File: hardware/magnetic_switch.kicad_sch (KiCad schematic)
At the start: 15 parts, among them J1 Conn_01x01_Socket, J2 Conn_01x01_Socket, J3 Conn_01x01_Socket, J4 Conn_01x01_Socket, Q1 SiA449DJ, Q2 BC847W, U1 DRV5012, U2 TPS70933

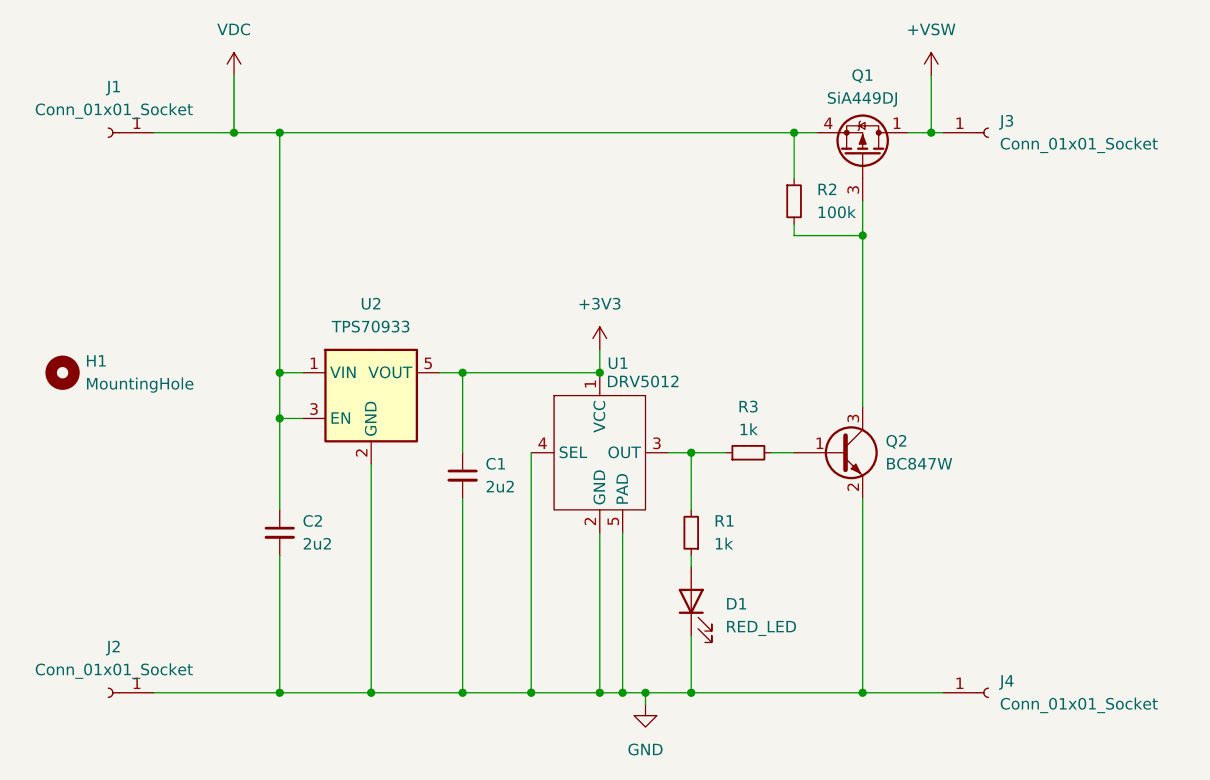
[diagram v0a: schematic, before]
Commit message: Minor cleanup of the schematic
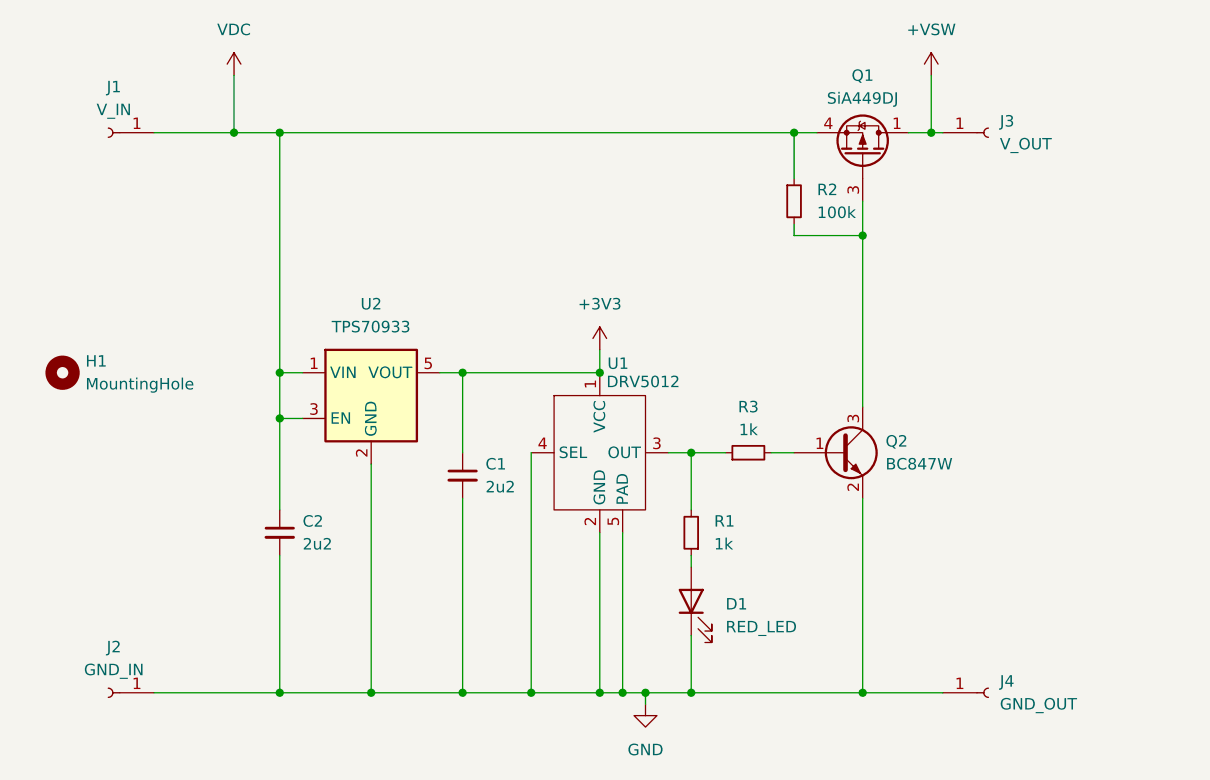
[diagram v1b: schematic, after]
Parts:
- J1: value Conn_01x01_Socket -> V_IN
- J2: value Conn_01x01_Socket -> GND_IN
- J3: value Conn_01x01_Socket -> V_OUT
- J4: value Conn_01x01_Socket -> GND_OUT
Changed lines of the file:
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@@
 			)
 		)
-		(property "Value" "Conn_01x01_Socket"
+		(property "Value" "GND_IN"
 			(at 59.055 97.79 0)
 			(effects
@@
 			)
 		)
-		(property "Value" "Conn_01x01_Socket"
+		(property "Value" "V_OUT"
 			(at 157.48 39.3699 0)
 			(effects
@@
 			)
 		)
-		(property "Value" "Conn_01x01_Socket"
+		(property "Value" "GND_OUT"
 			(at 157.48 101.5999 0)
 			(effects
@@
 			)
 		)
-		(property "Value" "Conn_01x01_Socket"
+		(property "Value" "V_IN"
 			(at 59.055 35.56 0)
 			(effects

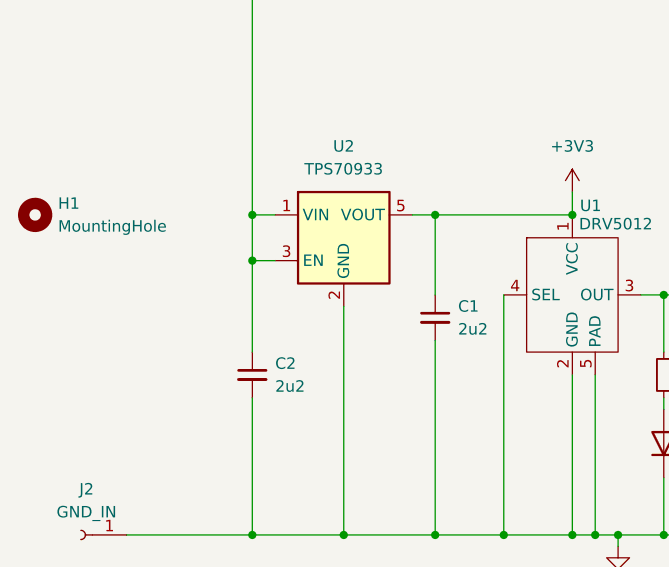
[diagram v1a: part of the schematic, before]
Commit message: Corrected issue with regulator enable pin which needs to be left floating, NOT tied to VCC and updated README to reflect the fact that testing is complete.
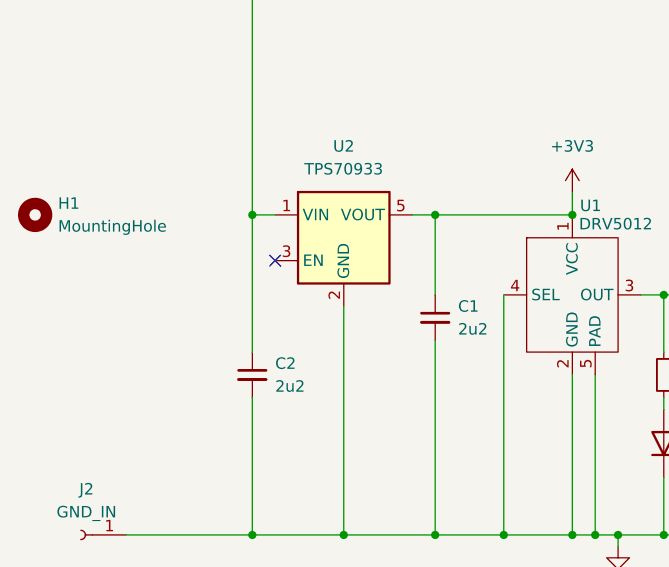
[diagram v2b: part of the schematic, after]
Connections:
- net VDC: no longer U2.3 (EN)
- no-connect marks 0 -> 1
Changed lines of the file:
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@@
-	)
-	(junction
-		(at 77.47 69.85)
-		(diameter 0)
-		(color 0 0 0 0)
 	)
 	(junction
@@
 		(color 0 0 0 0)
 	)
+	(no_connect
+		(at 80.01 69.85)
+	)
 	(wire
 		(pts
@@
 	(wire
 		(pts
-			(xy 77.47 69.85) (xy 77.47 64.77)
+			(xy 77.47 64.77) (xy 77.47 80.01)
 		)
 		(stroke
@@
 		)
 		(stroke
-			(width 0)
-			(type default)
-		)
-	)
-	(wire
-		(pts
-			(xy 80.01 69.85) (xy 77.47 69.85)
-		)
-		(stroke
-			(width 0)
-			(type default)
-		)
-	)
-	(wire
-		(pts
-			(xy 77.47 69.85) (xy 77.47 80.01)
-		)
-		(stroke

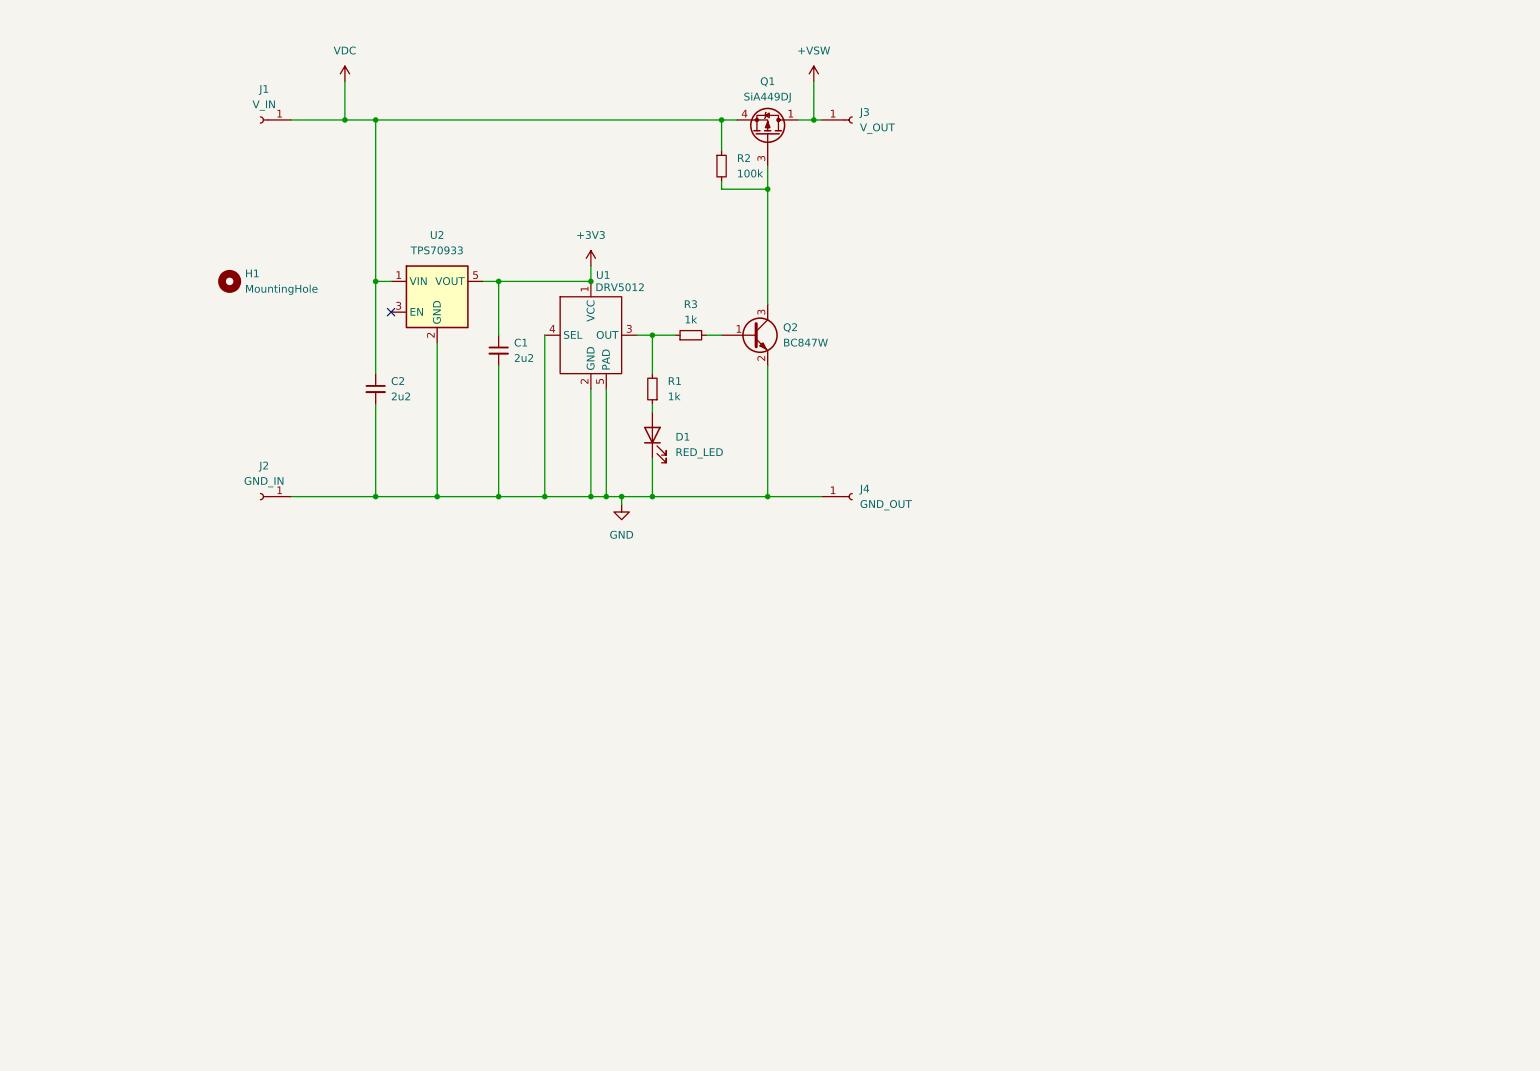
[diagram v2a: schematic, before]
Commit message: updated to smaller components and re-layed out.
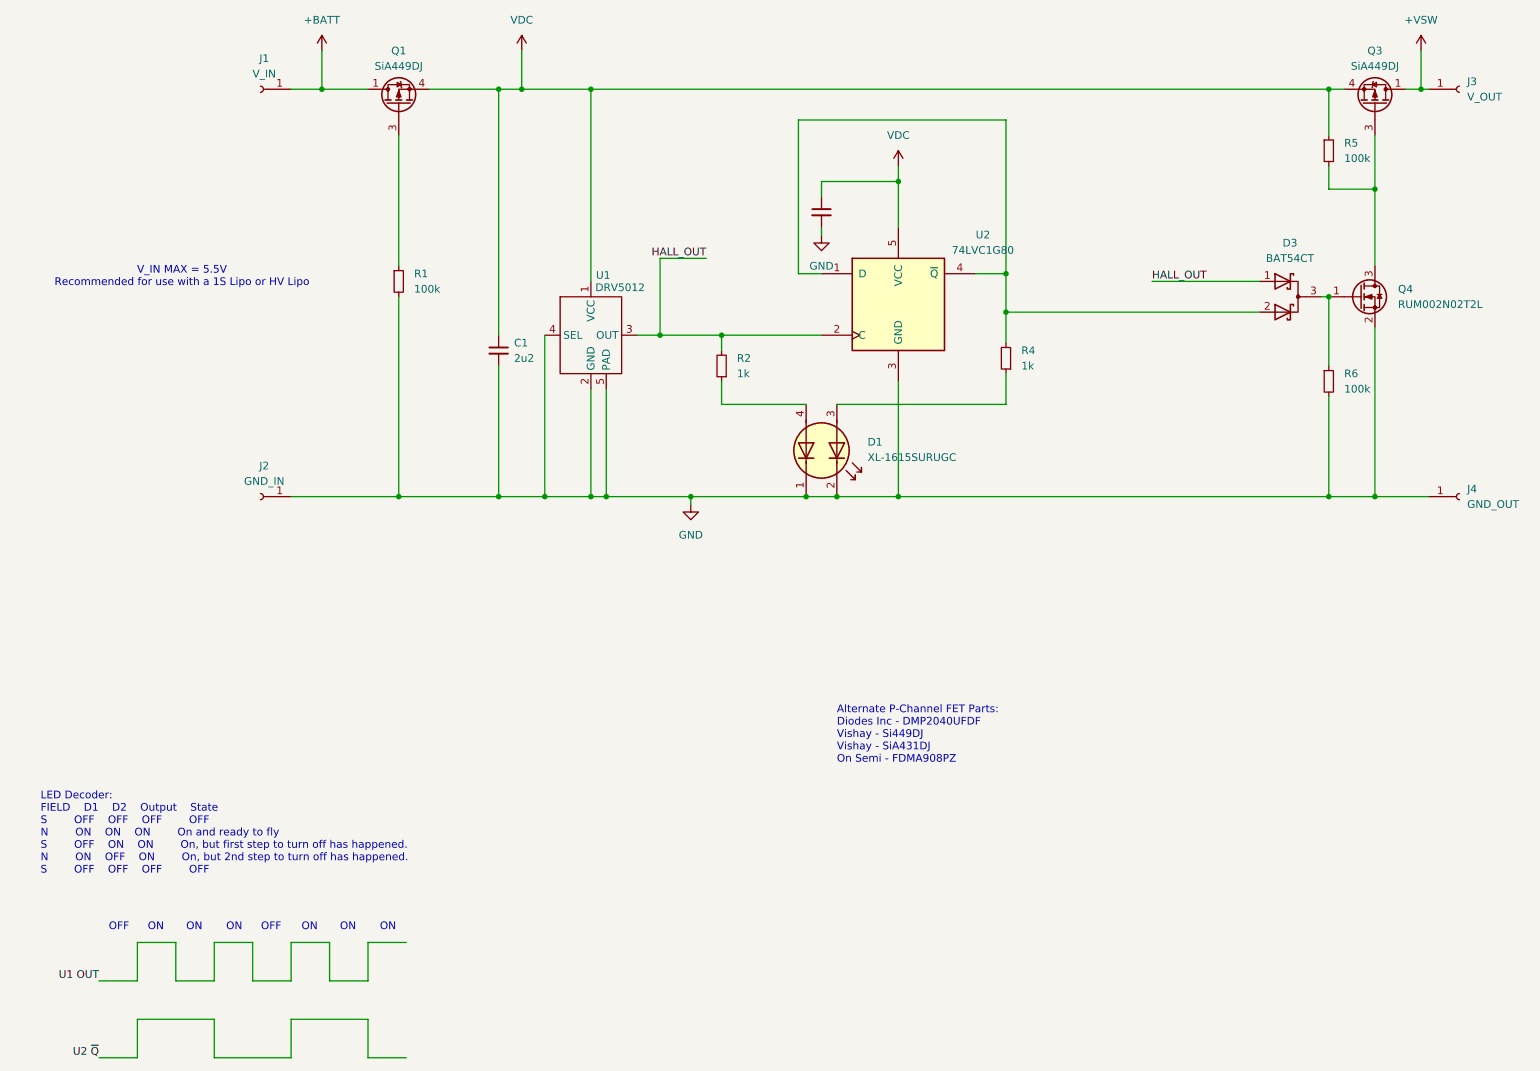
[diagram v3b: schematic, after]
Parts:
- removed D1: RED_LED, LED_SMD:LED_0402_1005Metric, symbol Device:LED
- removed H1: MountingHole, MountingHole:MountingHole_2.2mm_M2_DIN965_Pad, symbol Mechanical:MountingHole
- removed Q2: BC847W, Package_TO_SOT_SMD:SOT-323_SC-70, symbol Transistor_BJT:BC847W
- removed R3: 1k, Resistor_SMD:R_0402_1005Metric, symbol Device:R_Small
- removed U2: TPS70933, Package_TO_SOT_SMD:SOT-23-5, symbol Regulator_Linear:NCP163ASN330T1G
- added D1: XL-1615SURUGC, Footprints:LED_SMT_DUAL_1615, symbol My Components:LED_Dual_KKAA
- added D3: BAT54CT, Package_TO_SOT_SMD:SOT-523, symbol Device:D_Schottky_Dual_CommonCathode_AAK_Parallel
- added Q1: SiA449DJ, Package_TO_SOT_SMD:Vishay_PowerPAK_SC70-6L_Single, symbol Transistor_FET:SiA449DJ
- added Q4: RUM002N02T2L, Package_TO_SOT_SMD:SOT-723, symbol Transistor_FET:Q_NMOS_GSD
- added R1, R6: 100k, Resistor_SMD:R_0402_1005Metric, symbol Device:R_Small
- added R4: 1k, Resistor_SMD:R_0402_1005Metric, symbol Device:R_Small
- added U2: 74LVC1G80, Package_TO_SOT_SMD:SOT-353_SC-70-5, symbol 74xGxx:74LVC1G80
- C2: value 2u2 -> 100n
- J1, J2, J3, J4: footprint My Footprints:WireSolderPad_w_hole -> MountingHole:MountingHole_2.2mm_M2_DIN965_Pad
- U1: footprint My Footprints:X2SON_4_EP -> Footprints:X2SON_4_EP
- renumbered Q1 to Q3, R1 to R2, R2 to R5
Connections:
- net +3V3 is gone; now on net VDC: C1.1, U1.1 (VCC)
- net GND: now also D1.1 (K2), D1.2 (K1), Q4.2 (S), R1.2, R6.2, U2.3 (GND)
- net VDC: now also Q1.4 (S), U2.5 (VCC); no longer J1.1 (Pin_1)
- net at R2.1: now also D1.4 (A2)
- net HALL_OUT: now reaches R2.2, U1.3 (OUT)
- net HALL_OUT: now also D3.1 (A), U2.2 (C)
- net at Q3.3 (G), R5.2: now also Q4.3 (D)
- new net: D1.3 (A1), R4.1
- new net: D3.2 (A), R4.2, U2.1 (D), U2.4 (~{Q})
- new net: D3.3 (K), Q4.1 (G), R6.1
- new net: Q1.3 (G), R1.1
- new net +BATT: J1.1 (Pin_1), Q1.1 (D)
- no-connect marks 1 -> 0
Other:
- note added: "Alternate P-Channel FET Parts: Diodes Inc - DMP2040UFDF Vishay - Si449DJ Vishay - SiA431DJ On Semi - FDMA908PZ"
- note added: "LED Decoder: FIELD D1 D2 Output State S OFF OFF OFF OFF N ON ON ON On and ready to fly S OFF ON ON On, but first step to turn off has happened. N ON OFF ON On, but 2nd step to turn off has happened. S OFF OFF OFF OFF"
- note added: "OFF"
- note added: "ON"
- note added: "V_IN MAX = 5.5V Recommended for use with a 1S Lipo or HV Lipo"
- title: SimpleSwitch -> MagSafeSwitch
- moved on the sheet: J1, J3, J4, Q3, R2, R5

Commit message: added a linear regulator to allow up to +12V input. This version was sent for manufacture.
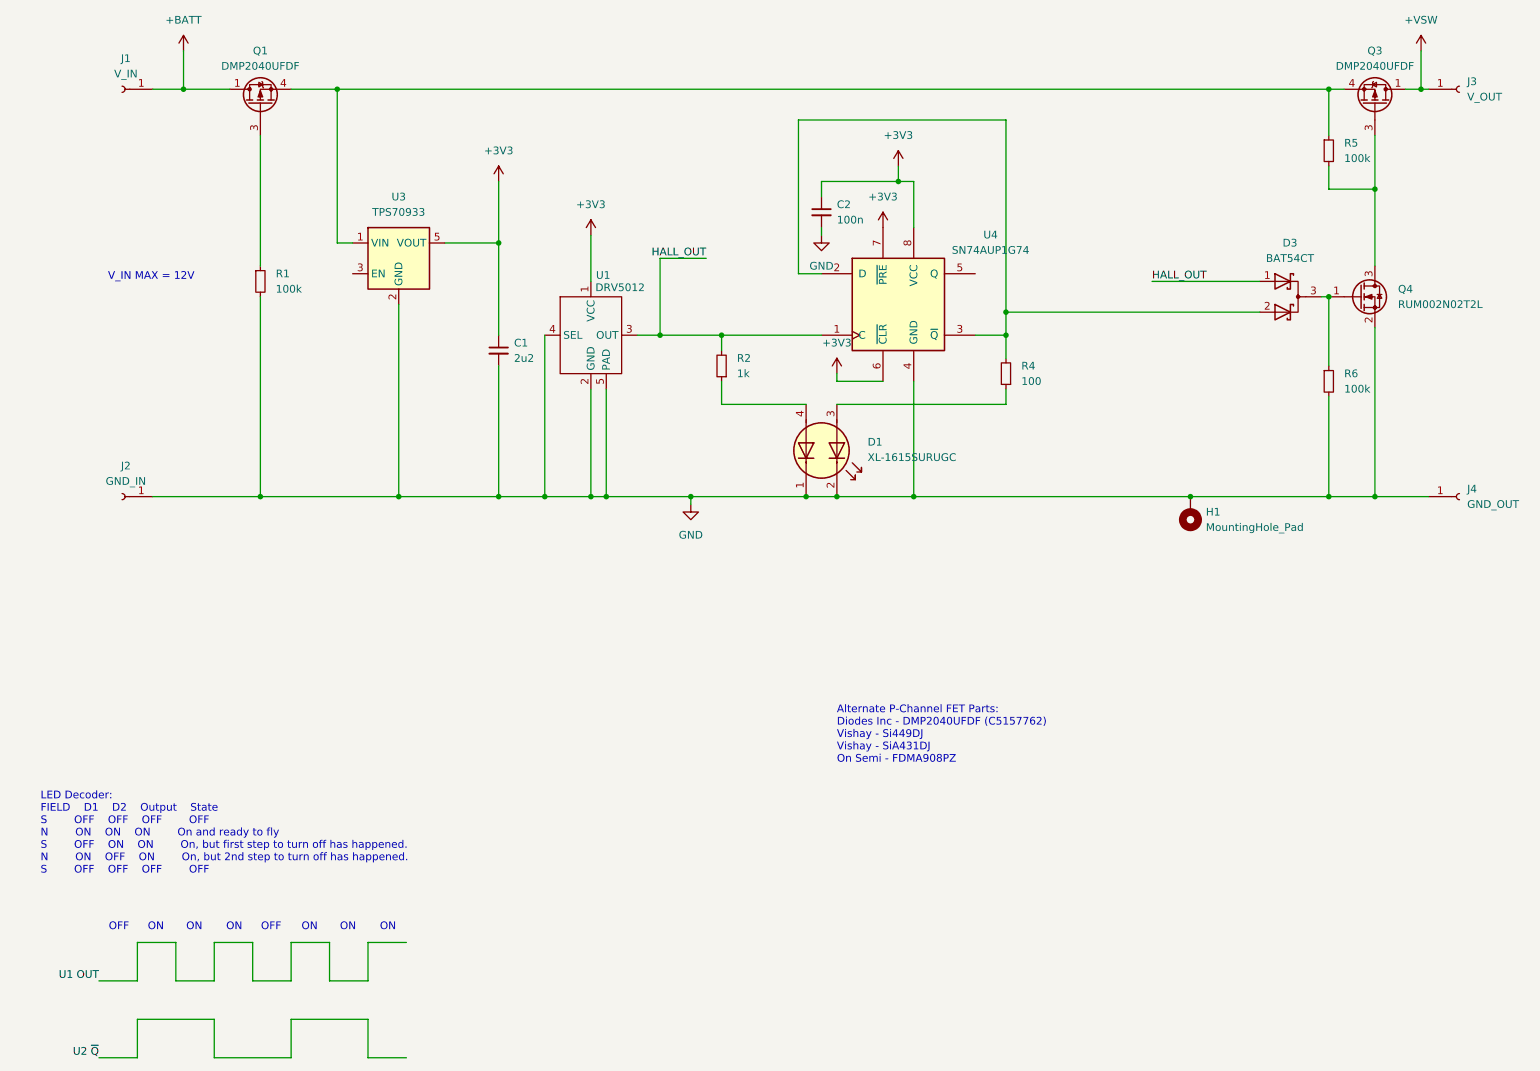
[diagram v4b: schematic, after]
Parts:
- removed U2: 74LVC1G80, Package_TO_SOT_SMD:SOT-353_SC-70-5, symbol 74xGxx:74LVC1G80
- added H1: MountingHole_Pad, MountingHole:MountingHole_2.2mm_M2_DIN965_Pad, symbol Mechanical:MountingHole_Pad
- added U3: TPS70933, Package_TO_SOT_SMD:SOT-23-5, symbol Regulator_Linear:NCP163ASN330T1G
- added U4: SN74AUP1G74, Package_SON:X2SON-8_1.4x1mm_P0.35mm, symbol 74xGxx:74AUP1G74
- D1: JLCPCB Part # (none) -> C965839
- D3: JLCPCB Part # (none) -> C134407
- J1, J2, J3, J4: footprint MountingHole:MountingHole_2.2mm_M2_DIN965_Pad -> Footprints:WireSolderPad_w_hole
- Q1, Q3: value SiA449DJ -> DMP2040UFDF; JLCPCB Part # (none) -> C5157762
- Q4: JLCPCB Part # (none) -> C250130
- R4: value 1k -> 100
- U1: JLCPCB Part # (none) -> C2655038
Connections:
- net GND: now also H1.1, U3.2 (GND), U4.4 (GND)
- net HALL_OUT: now also U4.1 (C)
- net at D3.2 (A), R4.2: now also U4.2 (D), U4.3 (~{Q})
- net VDC: no longer names the net of Q1.4 (S), Q3.4 (S), R5.1
- net VDC: now also U3.1 (VIN); no longer C1.1, C2.1, U1.1 (VCC)
- new net +3V3: C1.1, C2.1, U1.1 (VCC), U3.5 (VOUT), U4.6 (~{CLR}), U4.7 (~{PRE}), U4.8 (VCC)
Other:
- note added: "Alternate P-Channel FET Parts: Diodes Inc - DMP2040UFDF (C5157762) Vishay - Si449DJ Vishay - SiA431DJ On Semi - FDMA908PZ"
- note added: "V_IN MAX = 12V"
- note removed: "Alternate P-Channel FET Parts: Diodes Inc - DMP2040UFDF Vishay - Si449DJ Vishay - SiA431DJ On Semi - FDMA908PZ"
- note removed: "V_IN MAX = 5.5V Recommended for use with a 1S Lipo or HV Lipo"
- moved on the sheet: J1, J2, Q1, R1, R4
